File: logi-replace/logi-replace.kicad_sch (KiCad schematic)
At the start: 3 parts, among them J2 RCA, J3 RCA, J4 RCA

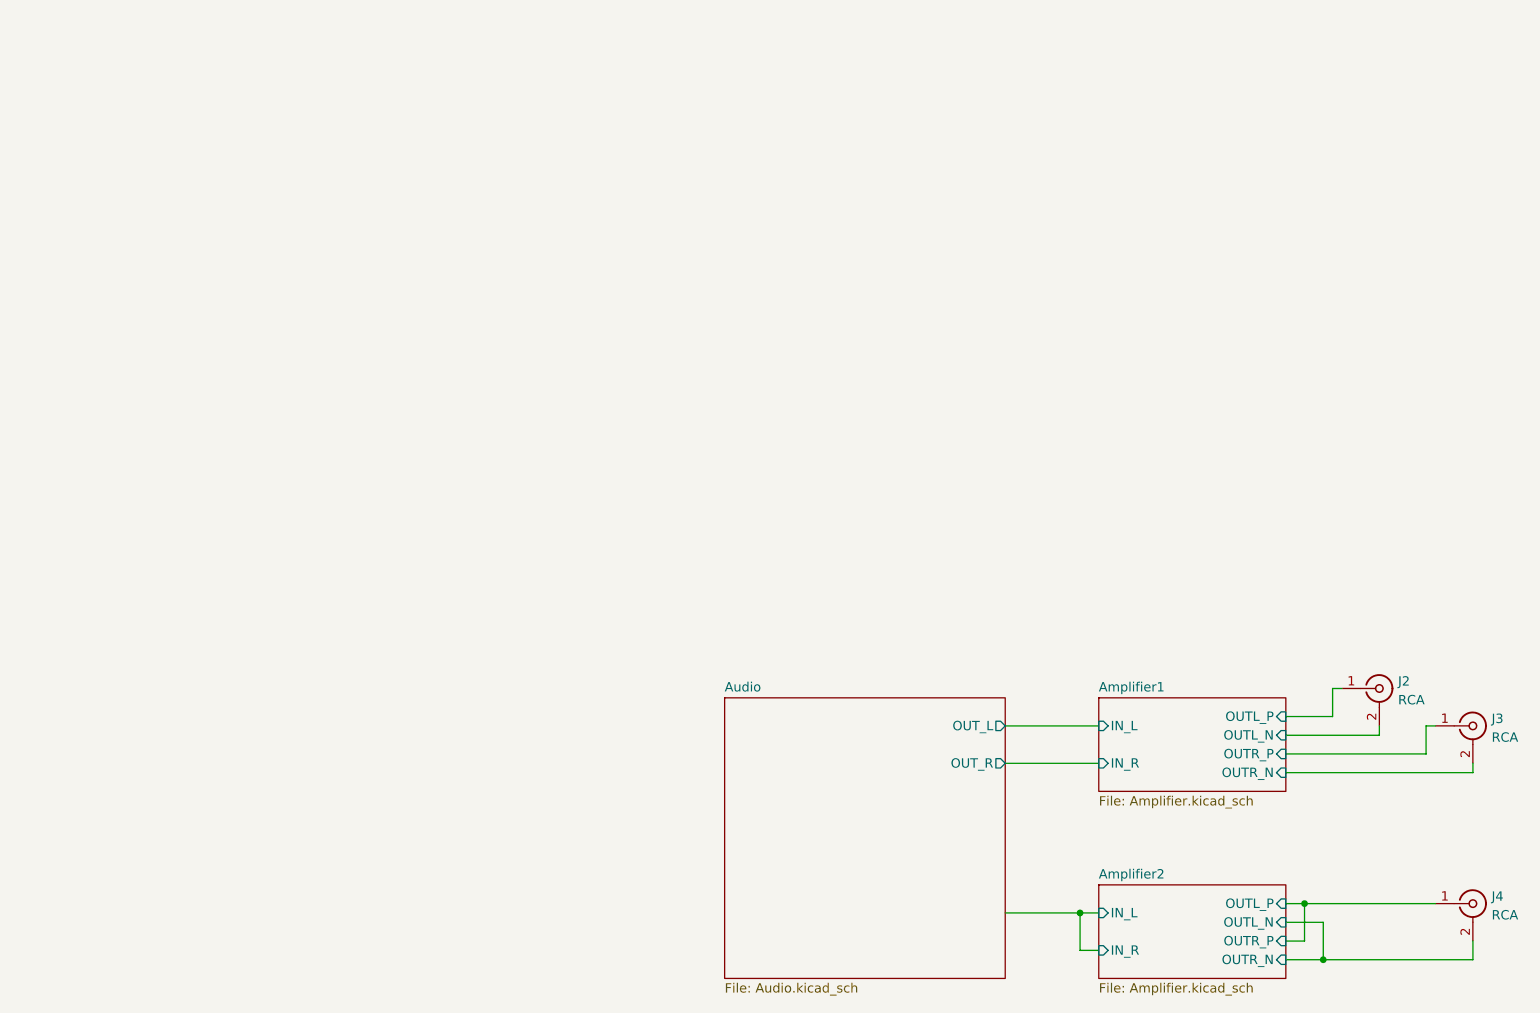
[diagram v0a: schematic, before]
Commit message: HW: Started work on the amplifier stages
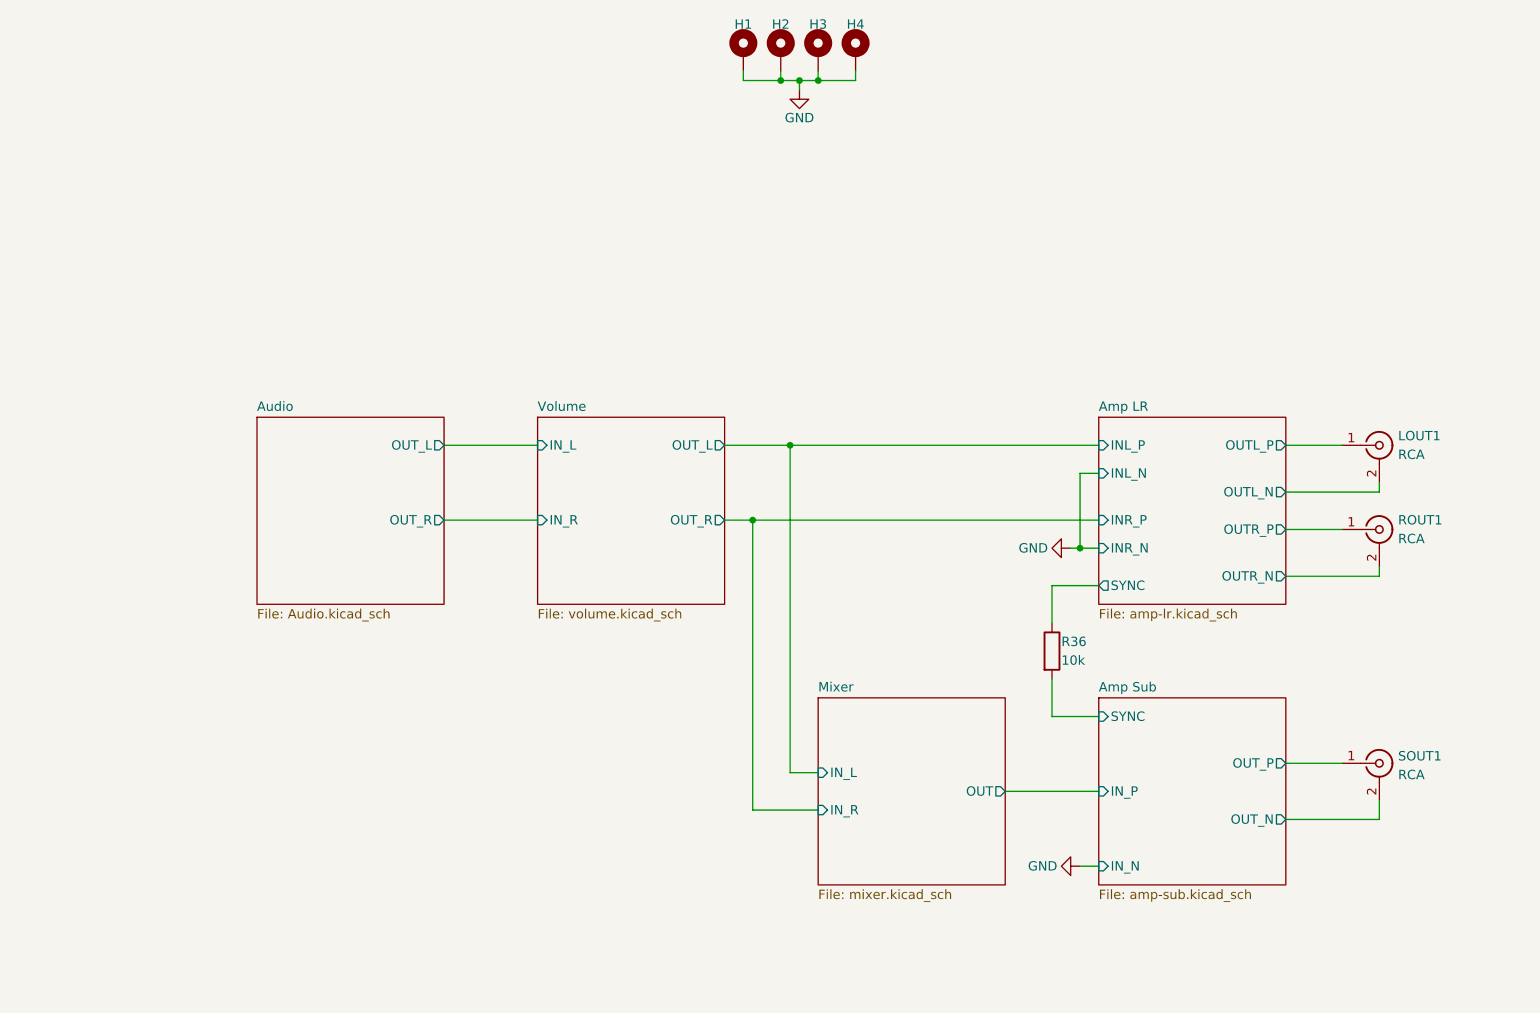
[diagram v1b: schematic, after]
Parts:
- added H1, H2, H3, H4: MountingHole_Pad, MountingHole:MountingHole_3.2mm_M3_Pad, symbol Mechanical:MountingHole_Pad
- added R36: 10k, Resistor_SMD:R_0402_1005Metric_Pad0.72x0.64mm_HandSolder, symbol Device:R
- LOUT1: renamed from J2; footprint (none) -> library:REAN_Black
- ROUT1: renamed from J3; footprint (none) -> library:REAN_Red
- renumbered J4 to SOUT1
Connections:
- net Amplifier1/OUTL_N renamed Amp LR/OUTL_N
- net Amplifier1/OUTL_P renamed Amp LR/OUTL_P
- net Amplifier1/OUTR_N renamed Amp LR/OUTR_N
- net Amplifier1/OUTR_P renamed Amp LR/OUTR_P
- net Amplifier2/OUTL_N renamed Amp Sub/OUT_N
- net Amplifier2/OUTL_P renamed Amp Sub/OUT_P
- new net Amp LR/SYNC: R36.1
- new net Amp Sub/SYNC: R36.2
- new net GND: H1.1, H2.1, H3.1, H4.1
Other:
- removed sheet Amplifier1
- removed sheet Amplifier2
- added sheet Amp LR (amp-lr.kicad_sch)
- added sheet Amp Sub (amp-sub.kicad_sch)
- added sheet Mixer (mixer.kicad_sch)
- added sheet Volume (volume.kicad_sch)
- moved on the sheet: LOUT1, ROUT1, SOUT1

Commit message: HW: Set board outlone and hole constraints
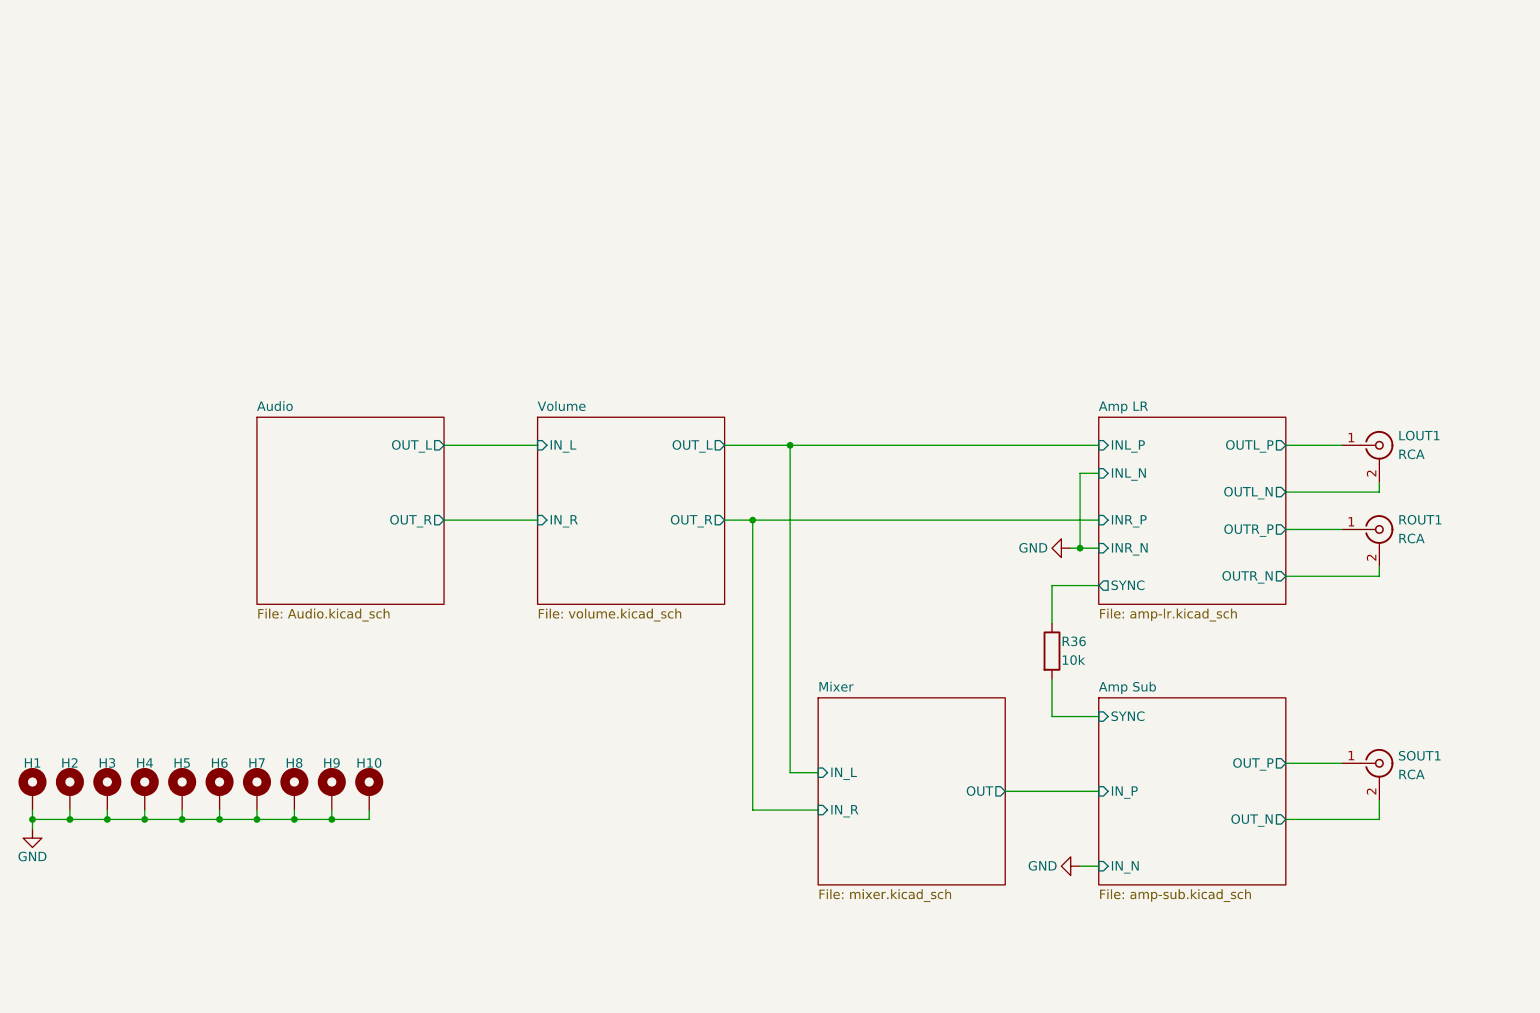
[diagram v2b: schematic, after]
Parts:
- added H10, H5, H6, H7, H8, H9: MountingHole_Pad, MountingHole:MountingHole_3.2mm_M3_Pad, symbol Mechanical:MountingHole_Pad
- R36: footprint Resistor_SMD:R_0402_1005Metric_Pad0.72x0.64mm_HandSolder -> Resistor_SMD:R_0603_1608Metric_Pad0.98x0.95mm_HandSolder
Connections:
- net GND: now also H10.1, H5.1, H6.1, H7.1, H8.1, H9.1
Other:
- moved on the sheet: H1, H2, H3, H4
